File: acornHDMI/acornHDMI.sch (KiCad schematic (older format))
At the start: 33 parts, among them J1 Conn_01x20_Shielded, J3 HDMI_A, U1 PTN3381B, U2 PCA9534

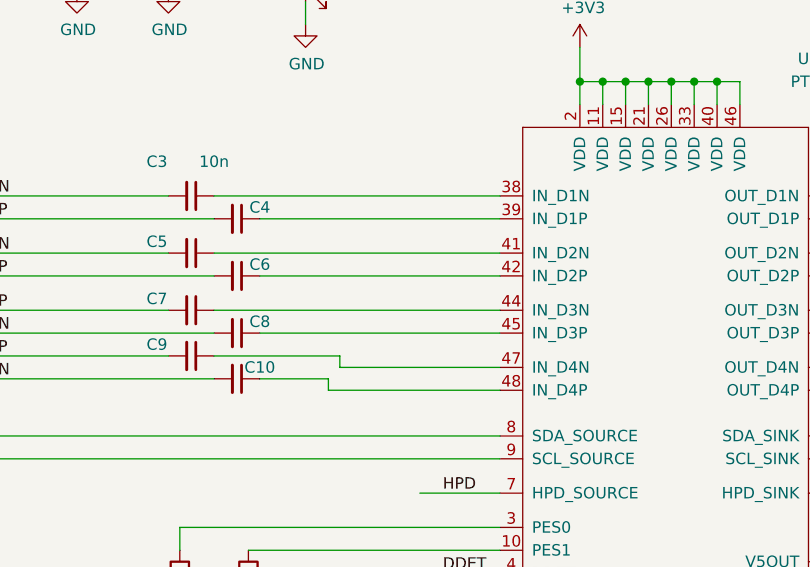
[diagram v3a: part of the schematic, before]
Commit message: a bit of routing. need to reconsider connector
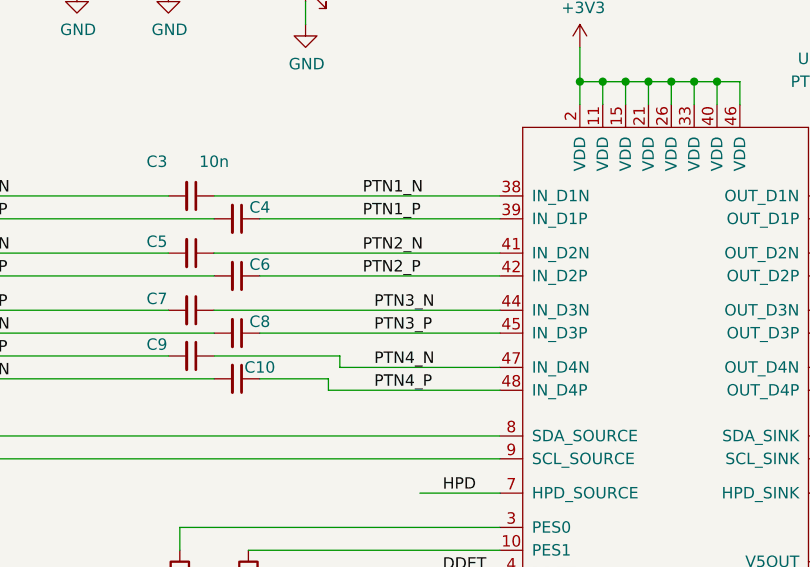
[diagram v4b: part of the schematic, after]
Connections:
- net labels added: PTN1_N, PTN1_P, PTN2_N, PTN2_P, PTN3_N, PTN3_P, PTN4_N, PTN4_P
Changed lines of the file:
@@
 Text Label 1700 4100 0    50   ~ 0
 INT_N
+Text Label 4900 3000 0    50   ~ 0
+PTN1_N
+Text Label 4900 3100 0    50   ~ 0
+PTN1_P
+Text Label 4900 3250 0    50   ~ 0
+PTN2_N
+Text Label 4900 3350 0    50   ~ 0
+PTN2_P
+Text Label 4950 3600 0    50   ~ 0
+PTN3_P
+Text Label 4950 3500 0    50   ~ 0
+PTN3_N
+Text Label 4950 3750 0    50   ~ 0
+PTN4_N
+Text Label 4950 3850 0    50   ~ 0
+PTN4_P
 $EndSCHEMATC

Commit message: add df52 to board. revise board edges, near finalization
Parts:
- J1: footprint local:3M_7700_20 -> localfp:DF52-20-S0.8H_handsoldering
- J3: footprint local:10029449-111 -> localfp:10029449-111
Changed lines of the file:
@@
 F 0 "J3" H 9880 3846 50  0000 L CNN
 F 1 "HDMI_A" H 9880 3755 50  0000 L CNN
-F 2 "local:10029449-111" H 9475 3800 50  0001 C CNN
+F 2 "localfp:10029449-111" H 9475 3800 50  0001 C CNN
 F 3 "https://en.wikipedia.org/wiki/HDMI" H 9475 3800 50  0001 C CNN
 	1    9450 3800
@@
 F 0 "J1" H 1072 4223 50  0000 C CNN
 F 1 "Conn_01x20_Shielded" H 1072 4224 50  0001 C CNN
-F 2 "local:3M_7700_20" H 1150 3200 50  0001 C CNN
+F 2 "localfp:DF52-20-S0.8H_handsoldering" H 1150 3200 50  0001 C CNN
 F 3 "~" H 1150 3200 50  0001 C CNN
 	1    1150 3200

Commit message: revA for initial production
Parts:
- added C13, C14, C15, C16, C17, C18, C19, C20, C21: 10n, Capacitor_SMD:C_0402_1005Metric_Pad0.74x0.62mm_HandSolder, symbol Device:C_Small
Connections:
- wire segments 232 -> 268
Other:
- note added: "Address b0100_000x: PCA\nAddress b1010_000x: EDID"
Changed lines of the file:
@@
 Text Label 4950 3850 0    50   ~ 0
 PTN4_P
+$Comp
+L Device:C_Small C13
+U 1 1 61A3F9A1
+P 6250 1600
+F 0 "C13" H 6100 1450 50  0000 C CNN
+F 1 "10n" H 6100 1700 50  0000 C CNN
+F 2 "Capacitor_SMD:C_0402_1005Metric_Pad0.74x0.62mm_HandSolder" H 6250 1600 50  0001 C CNN
+F 3 "~" H 6250 1600 50  0001 C CNN
+	1    6250 1600
+	-1   0    0    1
+$EndComp
+$Comp
+L Device:C_Small C14
+U 1 1 61A52352
+P 6600 1600
+F 0 "C14" H 6450 1450 50  0000 C CNN
+F 1 "10n" H 6450 1700 50  0000 C CNN
+F 2 "Capacitor_SMD:C_0402_1005Metric_Pad0.74x0.62mm_HandSolder" H 6600 1600 50  0001 C CNN
+F 3 "~" H 6600 1600 50  0001 C CNN
+	1    6600 1600
+	-1   0    0    1
+$EndComp
+$Comp
+L Device:C_Small C15
+U 1 1 61A529CB
+P 6950 1600
+F 0 "C15" H 6800 1450 50  0000 C CNN
+F 1 "10n" H 6800 1700 50  0000 C CNN
+F 2 "Capacitor_SMD:C_0402_1005Metric_Pad0.74x0.62mm_HandSolder" H 6950 1600 50  0001 C CNN
+F 3 "~" H 6950 1600 50  0001 C CNN
+	1    6950 1600
+	-1   0    0    1
+$EndComp
+$Comp
+L Device:C_Small C16
+U 1 1 61A52EAA
+P 7250 1600
+F 0 "C16" H 7100 1450 50  0000 C CNN
+F 1 "10n" H 7100 1700 50  0000 C CNN
+F 2 "Capacitor_SMD:C_0402_1005Metric_Pad0.74x0.62mm_HandSolder" H 7250 1600 50  0001 C CNN
+F 3 "~" H 7250 1600 50  0001 C CNN
+	1    7250 1600
+	-1   0    0    1
+$EndComp
+$Comp
+L Device:C_Small C17
+U 1 1 61A7DA34
+P 7550 1600
+F 0 "C17" H 7400 1450 50  0000 C CNN
+F 1 "10n" H 7400 1700 50  0000 C CNN
+F 2 "Capacitor_SMD:C_0402_1005Metric_Pad0.74x0.62mm_HandSolder" H 7550 1600 50  0001 C CNN
+F 3 "~" H 7550 1600 50  0001 C CNN
+	1    7550 1600
+	-1   0    0    1
+$EndComp
+$Comp
+L Device:C_Small C18
+U 1 1 61A7DC16
+P 7900 1600
+F 0 "C18" H 7750 1450 50  0000 C CNN
+F 1 "10n" H 7750 1700 50  0000 C CNN
+F 2 "Capacitor_SMD:C_0402_1005Metric_Pad0.74x0.62mm_HandSolder" H 7900 1600 50  0001 C CNN
+F 3 "~" H 7900 1600 50  0001 C CNN
+	1    7900 1600
+	-1   0    0    1
+$EndComp
+$Comp
+L Device:C_Small C19
+U 1 1 61A7DC20
+P 8250 1600
+F 0 "C19" H 8100 1450 50  0000 C CNN
+F 1 "10n" H 8100 1700 50  0000 C CNN
+F 2 "Capacitor_SMD:C_0402_1005Metric_Pad0.74x0.62mm_HandSolder" H 8250 1600 50  0001 C CNN
+F 3 "~" H 8250 1600 50  0001 C CNN
+	1    8250 1600
+	-1   0    0    1
+$EndComp
+$Comp
+L Device:C_Small C20
+U 1 1 61A7DC2A
+P 8550 1600
+F 0 "C20" H 8400 1450 50  0000 C CNN
+F 1 "10n" H 8400 1700 50  0000 C CNN
+F 2 "Capacitor_SMD:C_0402_1005Metric_Pad0.74x0.62mm_HandSolder" H 8550 1600 50  0001 C CNN
+F 3 "~" H 8550 1600 50  0001 C CNN
+	1    8550 1600
+	-1   0    0    1
+$EndComp
+$Comp
+L Device:C_Small C21
+U 1 1 61A9253C
+P 8850 1600
+F 0 "C21" H 8700 1450 50  0000 C CNN
+F 1 "10n" H 8700 1700 50  0000 C CNN
+F 2 "Capacitor_SMD:C_0402_1005Metric_Pad0.74x0.62mm_HandSolder" H 8850 1600 50  0001 C CNN
+F 3 "~" H 8850 1600 50  0001 C CNN
+	1    8850 1600
+	-1   0    0    1
+$EndComp
+$Comp
+L power:+3V3 #PWR01
+U 1 1 61A92AEC
+P 6250 1300
+F 0 "#PWR01" H 6250 1150 50  0001 C CNN
+F 1 "+3V3" H 6265 1473 50  0000 C CNN
+F 2 "" H 6250 1300 50  0001 C CNN
+F 3 "" H 6250 1300 50  0001 C CNN
+	1    6250 1300
+	1    0    0    -1
+$EndComp
+Wire Wire Line
+	6250 1300 6250 1350
+$Comp
+L power:GND #PWR02
+U 1 1 61AA5364
+P 6250 1900
+F 0 "#PWR02" H 6250 1650 50  0001 C CNN
+F 1 "GND" H 6255 1727 50  0000 C CNN
+F 2 "" H 6250 1900 50  0001 C CNN
+F 3 "" H 6250 1900 50  0001 C CNN
+	1    6250 1900
+	1    0    0    -1
+$EndComp
+Wire Wire Line
+	6250 1900 6250 1850
+Wire Wire Line
+	6600 1500 6600 1350
+Wire Wire Line
+	6600 1350 6250 1350
+Connection ~ 6250 1350
+Wire Wire Line
+	6250 1350 6250 1500
+Wire Wire Line
+	8850 1500 8850 1350
+Wire Wire Line
+	8850 1350 8550 1350
+Connection ~ 6600 1350
+Wire Wire Line
+	6950 1500 6950 1350
+Connection ~ 6950 1350
+Wire Wire Line
+	6950 1350 6600 1350
+Wire Wire Line
+	7250 1500 7250 1350
+Connection ~ 7250 1350
+Wire Wire Line
+	7250 1350 6950 1350
+Wire Wire Line
+	7550 1500 7550 1350
+Connection ~ 7550 1350
+Wire Wire Line
+	7550 1350 7250 1350
+Wire Wire Line
+	7900 1500 7900 1350
+Connection ~ 7900 1350
+Wire Wire Line
+	7900 1350 7550 1350
+Wire Wire Line
+	8250 1500 8250 1350
+Connection ~ 8250 1350
+Wire Wire Line
+	8250 1350 7900 1350
+Wire Wire Line
+	8550 1500 8550 1350
+Connection ~ 8550 1350
+Wire Wire Line
+	8550 1350 8250 1350
+Wire Wire Line
+	6600 1700 6600 1850
+Wire Wire Line
+	6600 1850 6250 1850
+Connection ~ 6250 1850
+Wire Wire Line
+	6250 1850 6250 1700
+Wire Wire Line
+	8850 1700 8850 1850
+Wire Wire Line
+	8850 1850 8550 1850
+Connection ~ 6600 1850
+Wire Wire Line
+	8550 1700 8550 1850
+Connection ~ 8550 1850
+Wire Wire Line
+	8550 1850 8250 1850
+Wire Wire Line
+	8250 1700 8250 1850
+Connection ~ 8250 1850
+Wire Wire Line
+	8250 1850 7900 1850
+Wire Wire Line
+	7900 1700 7900 1850
+Connection ~ 7900 1850
+Wire Wire Line
+	7900 1850 7550 1850
+Wire Wire Line
+	7550 1700 7550 1850
+Connection ~ 7550 1850
+Wire Wire Line
+	7550 1850 7250 1850
+Wire Wire Line
+	7250 1700 7250 1850
+Connection ~ 7250 1850
+Wire Wire Line
+	7250 1850 6950 1850
+Wire Wire Line
+	6950 1700 6950 1850
+Connection ~ 6950 1850
+Wire Wire Line
+	6950 1850 6600 1850
+Text Notes 1900 7250 0    79   ~ 0
+Address b0100_000x: PCA\nAddress b1010_000x: EDID
 $EndSCHEMATC
